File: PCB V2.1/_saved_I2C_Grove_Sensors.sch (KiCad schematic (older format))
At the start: 24 parts, among them J10 S4B-PH-SM4-TB(LF)(SN), J11 S4B-PH-SM4-TB(LF)(SN), J12 S4B-PH-SM4-TB(LF)(SN), J9 S4B-PH-SM4-TB(LF)(SN), U5 PCA9518DBQR

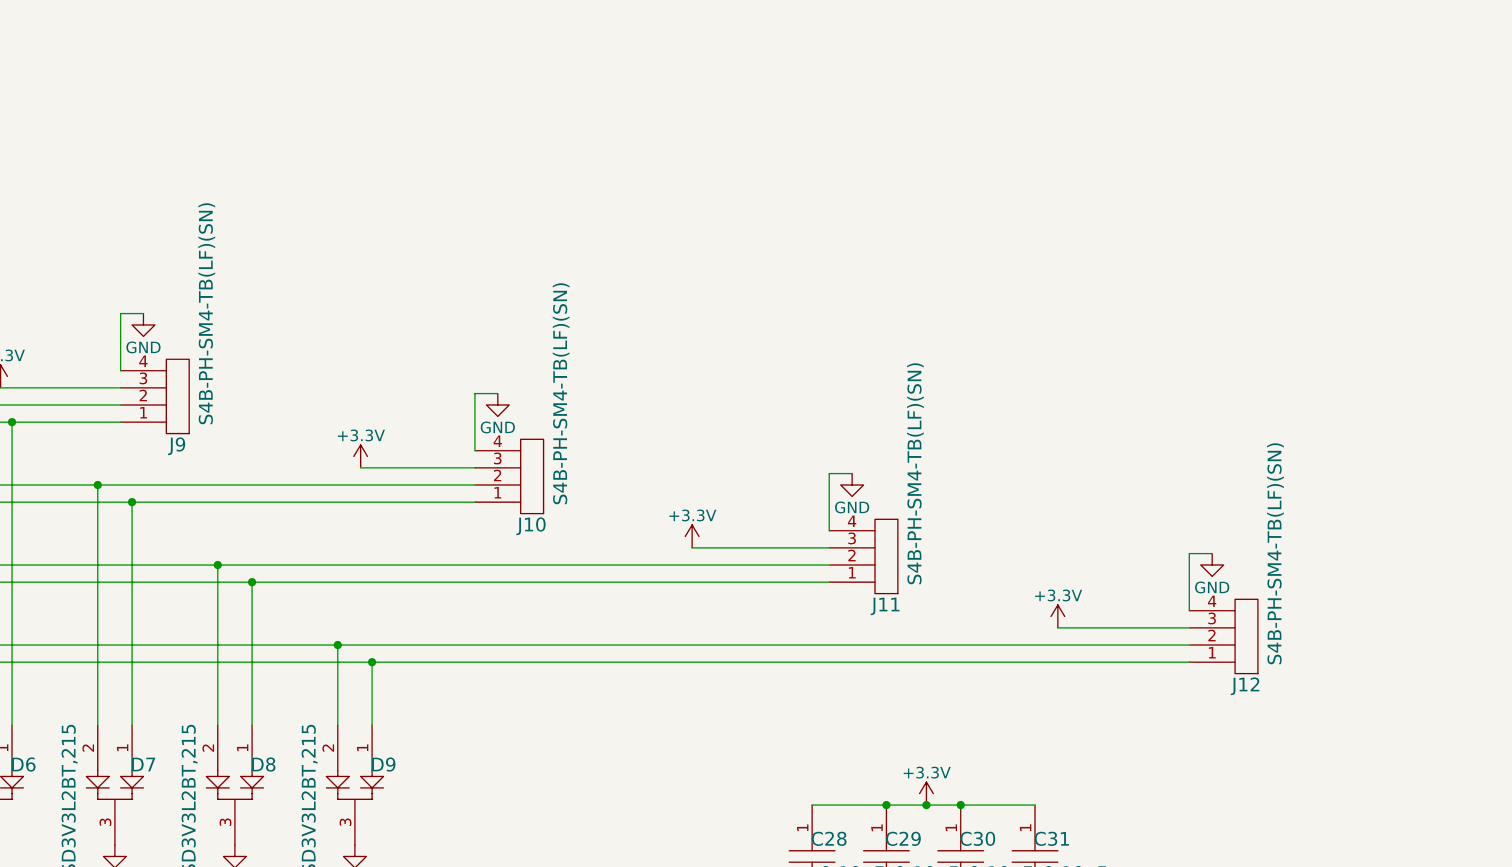
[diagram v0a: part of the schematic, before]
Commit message: Revert "Placement near completeq"
This reverts commit ae7bce2a0b52adb9ec10d03d9117548a28df5835.
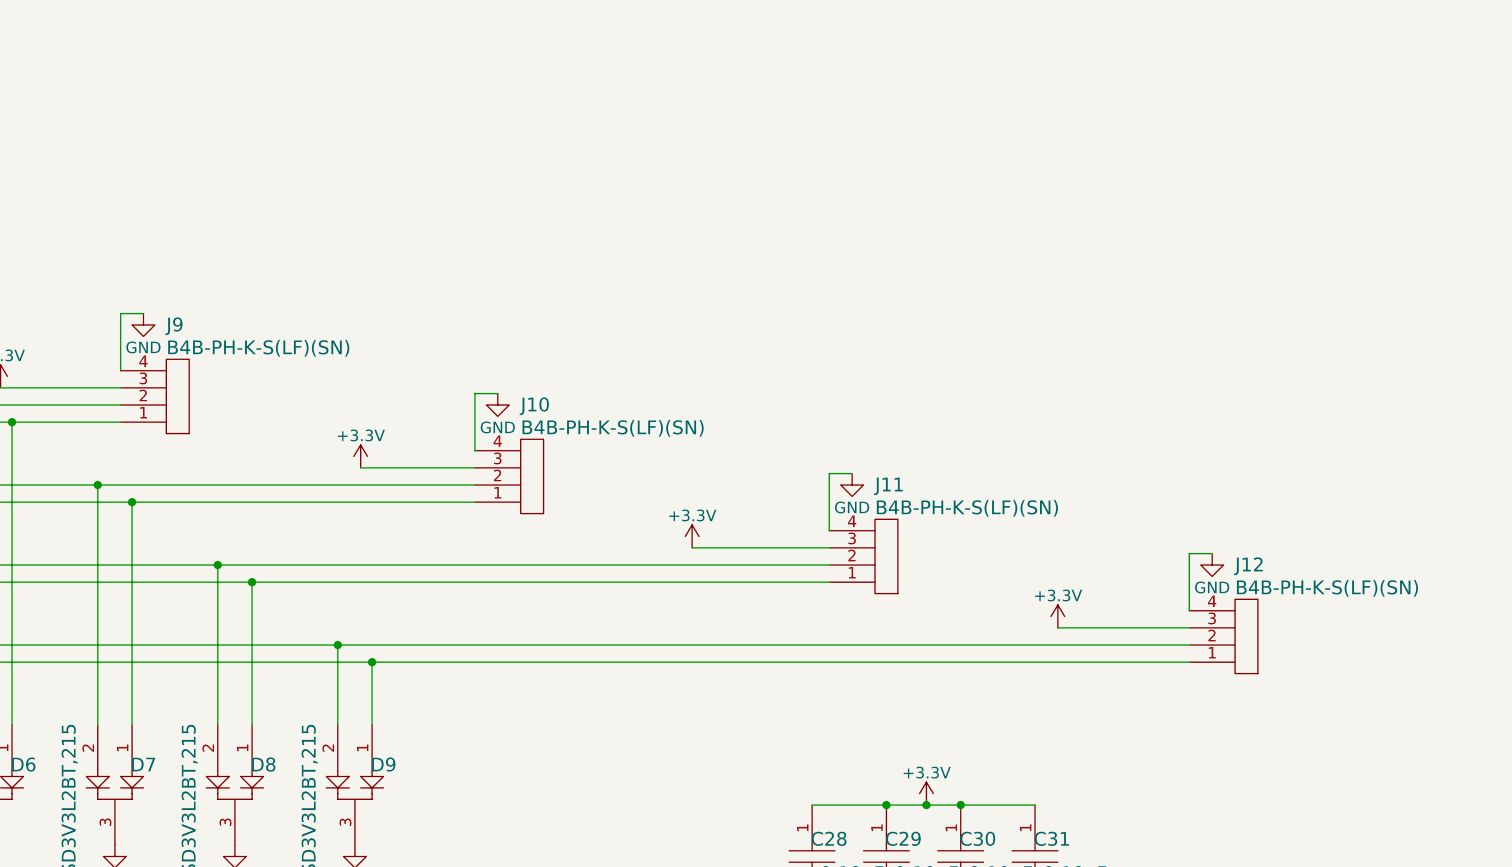
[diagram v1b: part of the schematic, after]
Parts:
- removed J10, J11, J12, J9: S4B-PH-SM4-TB(LF)(SN), PCB_Footprints:S4B-PH-SM4-TB(LF)(SN), symbol S4B-PH-SM4-TB(LF)(SN)
- added J10, J11, J12, J9: B4B-PH-K-S(LF)(SN), PCB_Footprints:B4B-PH-K-S(LF)(SN), symbol B4B-PH-K-S(LF)(SN)
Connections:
- net +3V3: now also J10.3, J11.3, J12.3, J9.3
- net GND: now also J10.4, J11.4, J12.4, J9.4
- net at D6.1, R28.2, U5.5 (SCL1): now also J9.1
- net at D6.2, R27.2, U5.6 (SDA1): now also J9.2
- net at D8.1, R32.2, U5.12 (SCL3): now also J11.1
- net at D8.2, R31.2, U5.13 (SDA3): now also J11.2
- net at D9.1, R34.2, U5.15 (SCL4): now also J12.1
- net at D9.2, R33.2, U5.16 (SDA4): now also J12.2
- net at D7.1, R30.2, U5.8 (SCL2): now also J10.1
- net at D7.2, R29.2, U5.9 (SDA2): now also J10.2
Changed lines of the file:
@@
 Connection ~ 1075 2650
 $Comp
-L S4B-PH-SM4-TB(LF)(SN) J9
-U 1 1 57DBA521
+L B4B-PH-K-S(LF)(SN) J9
+U 1 1 57DD0115
 P 6100 3800
-F 0 "J9" H 6050 3975 60  0000 C CNN
-F 1 "S4B-PH-SM4-TB(LF)(SN)" V 5925 3400 60  0000 C CNN
-F 2 "PCB_Footprints:S4B-PH-SM4-TB(LF)(SN)" H 5950 3875 60  0001 C CNN
+F 0 "J9" H 6100 3450 60  0000 R CNN
+F 1 "B4B-PH-K-S(LF)(SN)" H 6100 3550 60  0000 R CNN
+F 2 "PCB_Footprints:B4B-PH-K-S(LF)(SN)" H 5950 3875 60  0001 C CNN
 F 3 "http://www.jst-mfg.com/product/pdf/eng/ePH.pdf" H 5825 4175 60  0001 C CNN
-F 4 "0.32612 @ 5000" H 5925 4275 60  0001 C CNN "Cost"
+F 4 "0.09682 @ 5000" H 5925 4275 60  0001 C CNN "Cost"
 F 5 "9 Sept 2016" H 6025 4375 60  0001 C CNN "Date Created "
 F 6 "9 Sept 2016" H 6125 4475 60  0001 C CNN "Date Modified"
@@
 F 9 "Yes" H 6425 4775 60  0001 C CNN "RHoS?"
 F 10 "JST Sales America Inc" H 6525 4875 60  0001 C CNN "MFR"
-F 11 "S4B-PH-SM4-TB(LF)(SN)" H 6625 4975 60  0001 C CNN "MFR#"
-F 12 "SMT/SMD" H 6725 5075 60  0001 C CNN "Mounting"
+F 11 "B4B-PH-K-S(LF)(SN)" H 6625 4975 60  0001 C CNN "MFR#"
+F 12 "Through Hole" H 6725 5075 60  0001 C CNN "Mounting"
 F 13 "4" H 6825 5175 60  0001 C CNN "Pin Count#"
 F 14 "Active" H 6925 5275 60  0001 C CNN "Status"
 F 15 "N/A" H 7025 5375 60  0001 C CNN "Tolerance"
-F 16 "Surface Mount Right angle 4 pin connector" H 7125 5475 60  0001 C CNN "Type"
+F 16 "Through Hole vertical connector." H 7125 5475 60  0001 C CNN "Type"
 F 17 "N/A" H 7225 5575 60  0001 C CNN "Voltage"
 F 18 "N/A" H 7325 5675 60  0001 C CNN "Wattage"
@@
 $EndComp
 $Comp
-L S4B-PH-SM4-TB(LF)(SN) J10
-U 1 1 57DBA8B1
+L B4B-PH-K-S(LF)(SN) J10
+U 1 1 57DD0488
 P 7650 4150
-F 0 "J10" H 7600 4325 60  0000 C CNN
-F 1 "S4B-PH-SM4-TB(LF)(SN)" V 7475 3750 60  0000 C CNN
-F 2 "PCB_Footprints:S4B-PH-SM4-TB(LF)(SN)" H 7500 4225 60  0001 C CNN
+F 0 "J10" H 7650 3800 60  0000 R CNN
+F 1 "B4B-PH-K-S(LF)(SN)" H 7650 3900 60  0000 R CNN
+F 2 "PCB_Footprints:B4B-PH-K-S(LF)(SN)" H 7500 4225 60  0001 C CNN
 F 3 "http://www.jst-mfg.com/product/pdf/eng/ePH.pdf" H 7375 4525 60  0001 C CNN
-F 4 "0.32612 @ 5000" H 7475 4625 60  0001 C CNN "Cost"
+F 4 "0.09682 @ 5000" H 7475 4625 60  0001 C CNN "Cost"
 F 5 "9 Sept 2016" H 7575 4725 60  0001 C CNN "Date Created "
 F 6 "9 Sept 2016" H 7675 4825 60  0001 C CNN "Date Modified"
@@
 F 9 "Yes" H 7975 5125 60  0001 C CNN "RHoS?"
 F 10 "JST Sales America Inc" H 8075 5225 60  0001 C CNN "MFR"
-F 11 "S4B-PH-SM4-TB(LF)(SN)" H 8175 5325 60  0001 C CNN "MFR#"
-F 12 "SMT/SMD" H 8275 5425 60  0001 C CNN "Mounting"
+F 11 "B4B-PH-K-S(LF)(SN)" H 8175 5325 60  0001 C CNN "MFR#"
+F 12 "Through Hole" H 8275 5425 60  0001 C CNN "Mounting"
 F 13 "4" H 8375 5525 60  0001 C CNN "Pin Count#"
 F 14 "Active" H 8475 5625 60  0001 C CNN "Status"
 F 15 "N/A" H 8575 5725 60  0001 C CNN "Tolerance"
-F 16 "Surface Mount Right angle 4 pin connector" H 8675 5825 60  0001 C CNN "Type"
+F 16 "Through Hole vertical connector." H 8675 5825 60  0001 C CNN "Type"
 F 17 "N/A" H 8775 5925 60  0001 C CNN "Voltage"
 F 18 "N/A" H 8875 6025 60  0001 C CNN "Wattage"
@@
 $EndComp
 $Comp
-L S4B-PH-SM4-TB(LF)(SN) J11
-U 1 1 57DBAB29
+L B4B-PH-K-S(LF)(SN) J11
+U 1 1 57DD051B
 P 9200 4500
-F 0 "J11" H 9150 4675 60  0000 C CNN
-F 1 "S4B-PH-SM4-TB(LF)(SN)" V 9025 4100 60  0000 C CNN
-F 2 "PCB_Footprints:S4B-PH-SM4-TB(LF)(SN)" H 9050 4575 60  0001 C CNN
+F 0 "J11" H 9200 4150 60  0000 R CNN
+F 1 "B4B-PH-K-S(LF)(SN)" H 9200 4250 60  0000 R CNN
+F 2 "PCB_Footprints:B4B-PH-K-S(LF)(SN)" H 9050 4575 60  0001 C CNN
 F 3 "http://www.jst-mfg.com/product/pdf/eng/ePH.pdf" H 8925 4875 60  0001 C CNN
-F 4 "0.32612 @ 5000" H 9025 4975 60  0001 C CNN "Cost"
+F 4 "0.09682 @ 5000" H 9025 4975 60  0001 C CNN "Cost"
 F 5 "9 Sept 2016" H 9125 5075 60  0001 C CNN "Date Created "
 F 6 "9 Sept 2016" H 9225 5175 60  0001 C CNN "Date Modified"
@@
 F 9 "Yes" H 9525 5475 60  0001 C CNN "RHoS?"
 F 10 "JST Sales America Inc" H 9625 5575 60  0001 C CNN "MFR"
-F 11 "S4B-PH-SM4-TB(LF)(SN)" H 9725 5675 60  0001 C CNN "MFR#"
-F 12 "SMT/SMD" H 9825 5775 60  0001 C CNN "Mounting"
+F 11 "B4B-PH-K-S(LF)(SN)" H 9725 5675 60  0001 C CNN "MFR#"
+F 12 "Through Hole" H 9825 5775 60  0001 C CNN "Mounting"
 F 13 "4" H 9925 5875 60  0001 C CNN "Pin Count#"
 F 14 "Active" H 10025 5975 60  0001 C CNN "Status"
 F 15 "N/A" H 10125 6075 60  0001 C CNN "Tolerance"
-F 16 "Surface Mount Right angle 4 pin connector" H 10225 6175 60  0001 C CNN "Type"
+F 16 "Through Hole vertical connector." H 10225 6175 60  0001 C CNN "Type"
 F 17 "N/A" H 10325 6275 60  0001 C CNN "Voltage"
 F 18 "N/A" H 10425 6375 60  0001 C CNN "Wattage"
@@
 $EndComp
 $Comp
-L S4B-PH-SM4-TB(LF)(SN) J12
-U 1 1 57DBAE04
+L B4B-PH-K-S(LF)(SN) J12
+U 1 1 57DD078E
 P 10775 4850
-F 0 "J12" H 10725 5025 60  0000 C CNN
-F 1 "S4B-PH-SM4-TB(LF)(SN)" V 10600 4450 60  0000 C CNN
-F 2 "PCB_Footprints:S4B-PH-SM4-TB(LF)(SN)" H 10625 4925 60  0001 C CNN
+F 0 "J12" H 10775 4500 60  0000 R CNN
+F 1 "B4B-PH-K-S(LF)(SN)" H 10775 4600 60  0000 R CNN
+F 2 "PCB_Footprints:B4B-PH-K-S(LF)(SN)" H 10625 4925 60  0001 C CNN
 F 3 "http://www.jst-mfg.com/product/pdf/eng/ePH.pdf" H 10500 5225 60  0001 C CNN
-F 4 "0.32612 @ 5000" H 10600 5325 60  0001 C CNN "Cost"
+F 4 "0.09682 @ 5000" H 10600 5325 60  0001 C CNN "Cost"
 F 5 "9 Sept 2016" H 10700 5425 60  0001 C CNN "Date Created "
 F 6 "9 Sept 2016" H 10800 5525 60  0001 C CNN "Date Modified"
@@
 F 9 "Yes" H 11100 5825 60  0001 C CNN "RHoS?"
 F 10 "JST Sales America Inc" H 11200 5925 60  0001 C CNN "MFR"
-F 11 "S4B-PH-SM4-TB(LF)(SN)" H 11300 6025 60  0001 C CNN "MFR#"
-F 12 "SMT/SMD" H 11400 6125 60  0001 C CNN "Mounting"
+F 11 "B4B-PH-K-S(LF)(SN)" H 11300 6025 60  0001 C CNN "MFR#"
+F 12 "Through Hole" H 11400 6125 60  0001 C CNN "Mounting"
 F 13 "4" H 11500 6225 60  0001 C CNN "Pin Count#"
 F 14 "Active" H 11600 6325 60  0001 C CNN "Status"
 F 15 "N/A" H 11700 6425 60  0001 C CNN "Tolerance"
-F 16 "Surface Mount Right angle 4 pin connector" H 11800 6525 60  0001 C CNN "Type"
+F 16 "Through Hole vertical connector." H 11800 6525 60  0001 C CNN "Type"
 F 17 "N/A" H 11900 6625 60  0001 C CNN "Voltage"
 F 18 "N/A" H 12000 6725 60  0001 C CNN "Wattage"
